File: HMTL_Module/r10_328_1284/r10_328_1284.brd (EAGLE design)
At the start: 79.7 x 61 mm, 40 parts, among them J2 AVR_SPI_PRG_6PTH, U2 ATMEGA328P_PDIP, Y1 20MHz

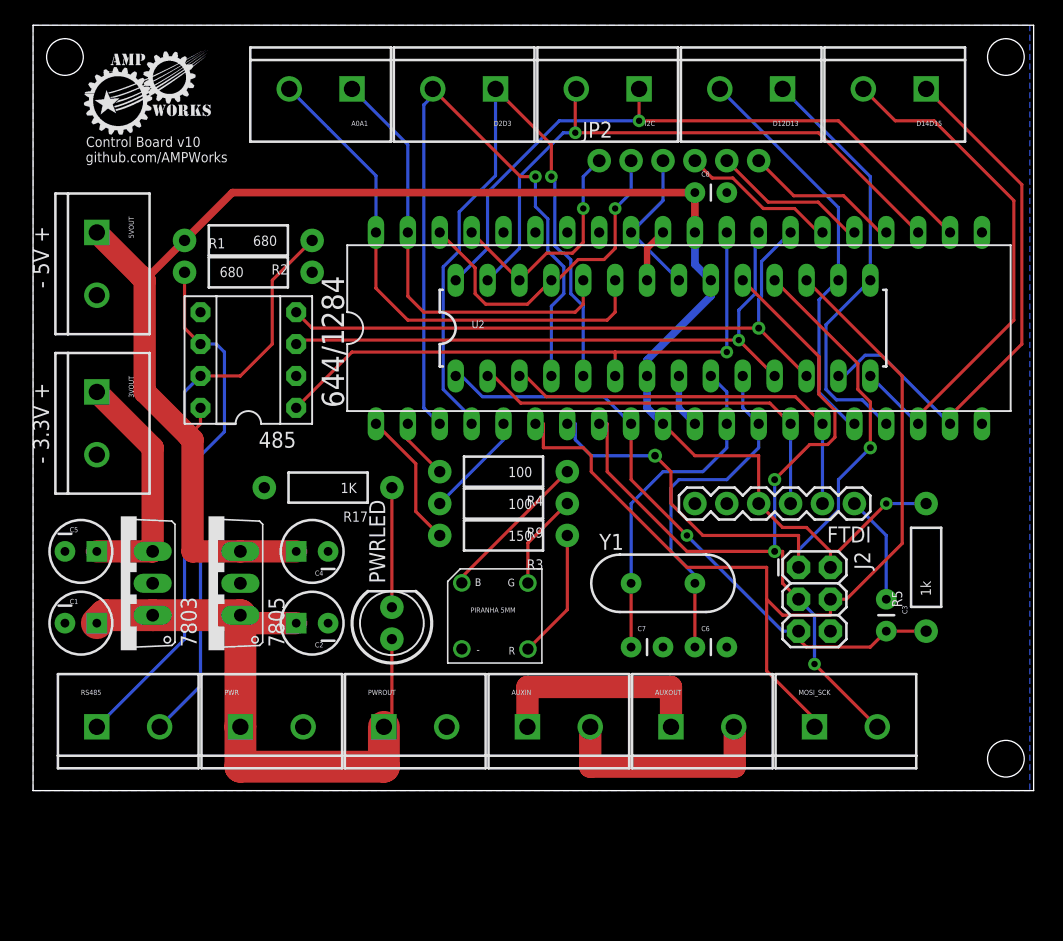
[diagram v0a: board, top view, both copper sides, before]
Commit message: For HTML 328/1284 module added LED for 328
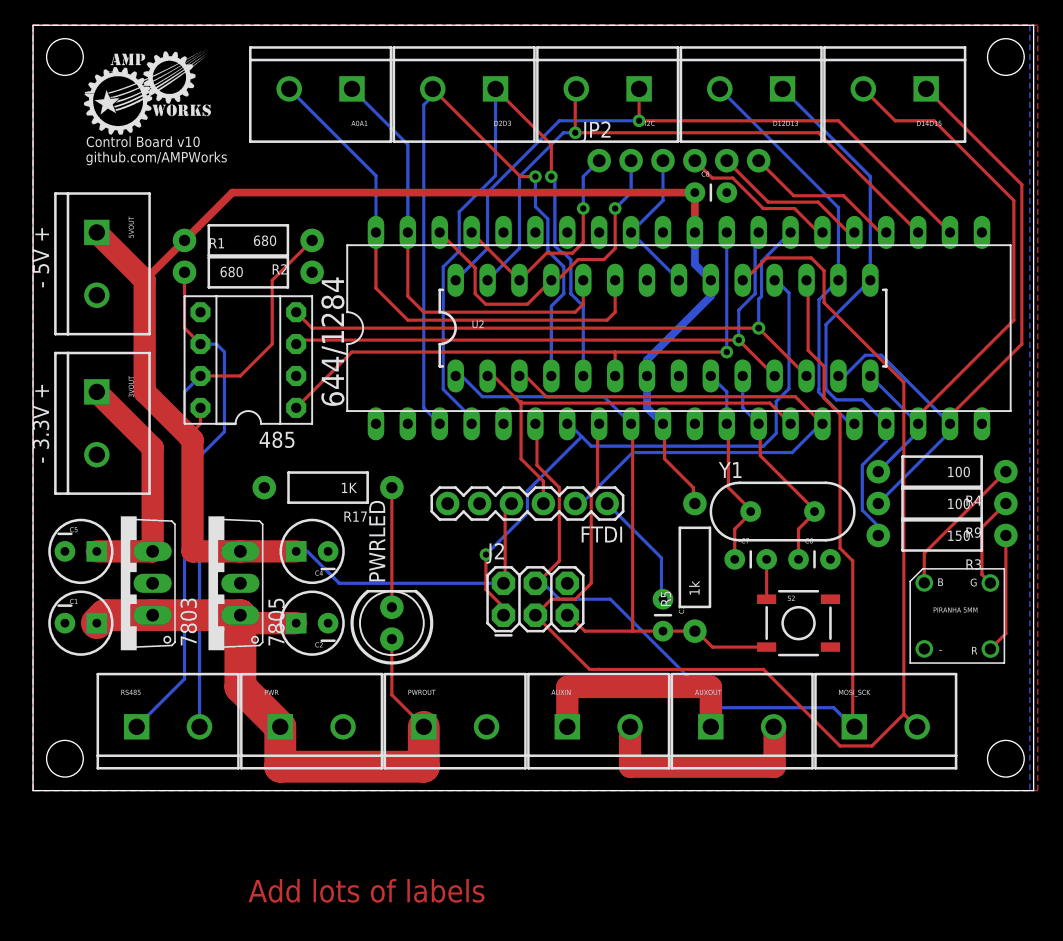
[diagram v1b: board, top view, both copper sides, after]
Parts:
- removed FRAME1: FRAME-LETTER, SparkFun-Aesthetics:CREATIVE_COMMONS
- added S2: Reset, SparkFun:TACTILE_SWITCH_SMD
- moved STATUS 36.8 mm to (73.7, 14.0)
- moved R3 34.9 mm to (72.4, 20.3)
- moved R4 34.9 mm to (72.4, 25.4)
- moved R9 34.9 mm to (72.4, 22.9)
- moved J2 23.8 mm to (37.5, 14.0), turned to 0 degrees
- moved FTDI 19.7 mm to (45.7, 22.9)
- moved R5 18.4 mm to (52.7, 17.8)
- moved C3 17.8 mm to (50.2, 15.2)
- moved Y1 11.1 mm to (59.7, 22.2)
- moved C6 10.8 mm to (61.0, 18.4)
- moved C7 10.8 mm to (55.9, 18.4)
- moved AUXIN 3.18 mm to (42.5, 5.08)
- moved AUXOUT 3.18 mm to (54.0, 5.08)
- moved MOSI_SCK 3.18 mm to (65.4, 5.08)
- moved RS485 3.18 mm to (8.26, 5.08)
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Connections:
- net D11D9: now also R3.P$2
- net D12D8: now also R4.P$2
- net D13D7: now also R9.P$2
- net GND: now also S2.1
- net LED1: no longer R3.P$2
- net LED2: no longer R4.P$2
- net LED3: no longer R9.P$2
- net RESET: now also S2.3
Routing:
- net SCK: track 65.6 -> 100.4 mm, vias 3 -> 0
- net TX: track 32.1 -> 48.0 mm
- net LED1: track 11.0 -> 0.00 mm
- net CLK1: track 27.1 -> 16.5 mm
- net CLK2: track 28.0 -> 17.6 mm
- net D11D9: track 34.2 -> 44.4 mm
- net D13D7: track 44.0 -> 52.7 mm
- net LED3: track 8.45 -> 0.00 mm
- net MISO: track 55.3 -> 49.0 mm, vias 2 -> 1
- net GND: track 8.67 -> 3.17 mm
- net D12D8: track 42.0 -> 47.1 mm
- net LED2: track 4.86 -> 0.00 mm
- net MOSI: track 77.8 -> 81.8 mm
- net RX: track 32.1 -> 34.7 mm
- net PWR+: track 50.3 -> 52.4 mm
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- added copper zone on layer 1, net GND
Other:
- board text added: "Add lots of labels"
